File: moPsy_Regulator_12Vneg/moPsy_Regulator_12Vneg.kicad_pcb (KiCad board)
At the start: 2 copper layers, 41 x 40 mm, 20 parts, among them J1 Conn_01x01_Male, J2 Conn_01x01_Male, J3 Conn_01x01_Male, J4 Conn_01x01_Male, U1 LT1185

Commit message: Add OSHW logo to Regulator 12V neg PCB
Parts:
- added REF**: OSHW-Logo2_7.3x6mm_SilkScreen, Symbol:OSHW-Logo2_7.3x6mm_SilkScreen, B.Cu at (114.3, 74.9)

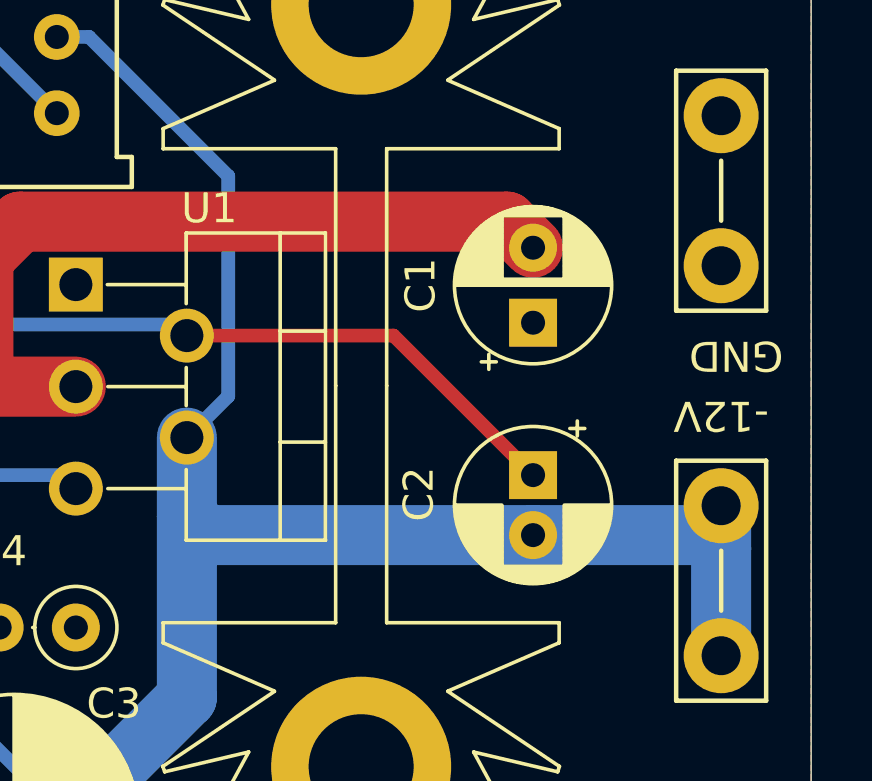
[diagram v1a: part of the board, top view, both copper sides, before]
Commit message: Put cap for -12V regulator on PCB
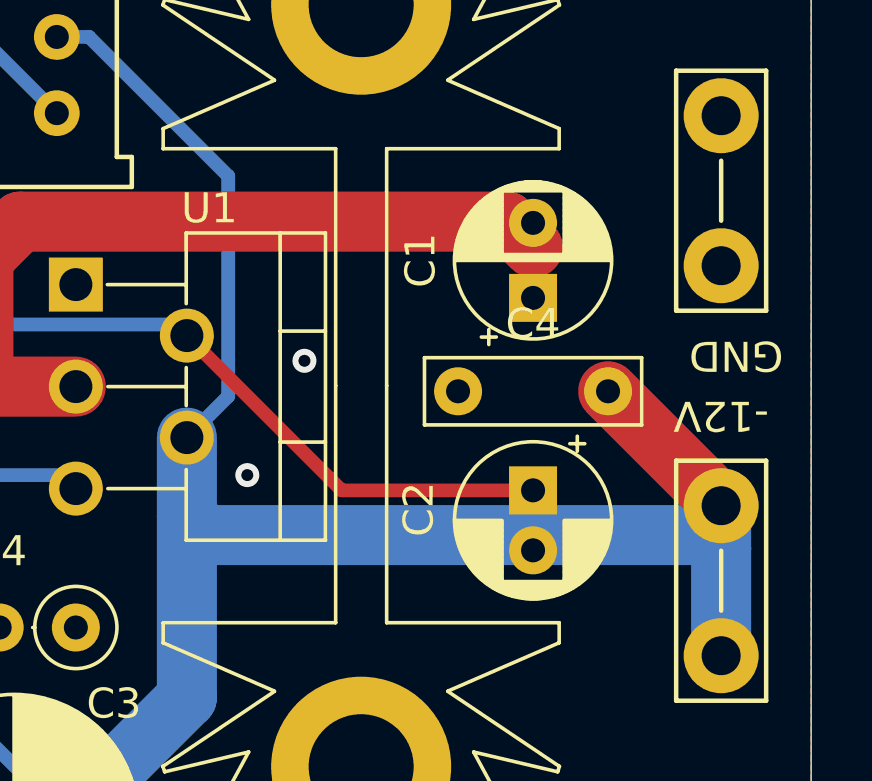
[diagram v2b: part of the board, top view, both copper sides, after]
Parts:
- added C4: 100n, Capacitor_THT:C_Rect_L7.0mm_W2.0mm_P5.00mm, F.Cu at (123.2, 91.2)
- moved C1 0.83 mm to (125.7, 88.1)
- moved C2 0.51 mm to (125.7, 94.5)
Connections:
- RV1 pad 3: (no net) -> unconnected-(RV1-Pad3)
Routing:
- net -12V: track 66.1 -> 71.4 mm
- net GND: vias 0 -> 2

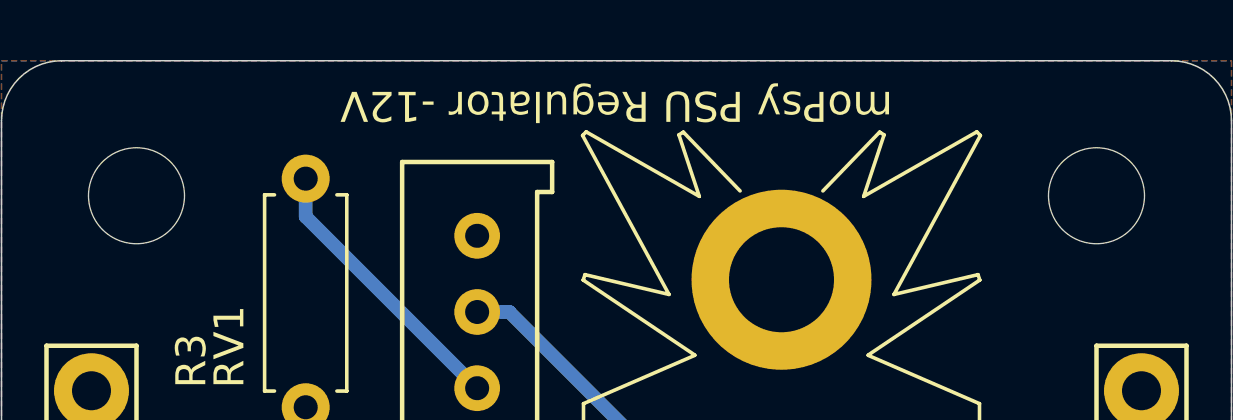
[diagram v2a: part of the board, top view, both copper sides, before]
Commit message: Advance board revision to 1.1
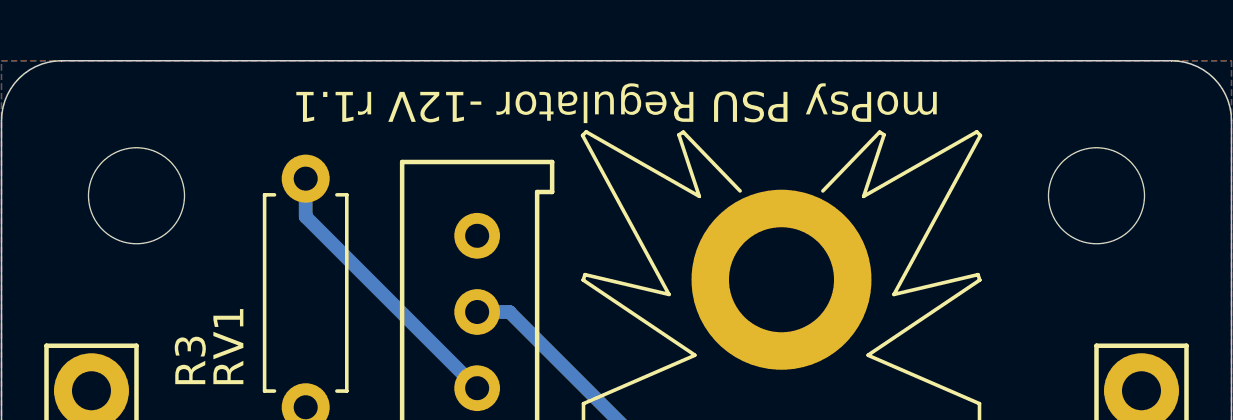
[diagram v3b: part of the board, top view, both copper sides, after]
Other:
- board text added: "moPsy PSU Regulator -12V r1.1"
- board text removed: "moPsy PSU Regulator -12V"
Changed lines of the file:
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@@
     (effects (font (size 1 1) (thickness 0.15)))
   )
-  (gr_text "moPsy PSU Regulator -12V" (at 114.5 72.5 180) (layer "F.SilkS")
+  (gr_text "moPsy PSU Regulator -12V r1.1" (at 114.5 72.5 180) (layer "F.SilkS")
     (effects (font (size 1 1) (thickness 0.15)))
   )
